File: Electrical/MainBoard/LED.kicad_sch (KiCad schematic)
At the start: 19 parts, among them U5 GSF7002DW, U6 GSF7002DW, U7 GSF7002DW, U8 GSF7002DW

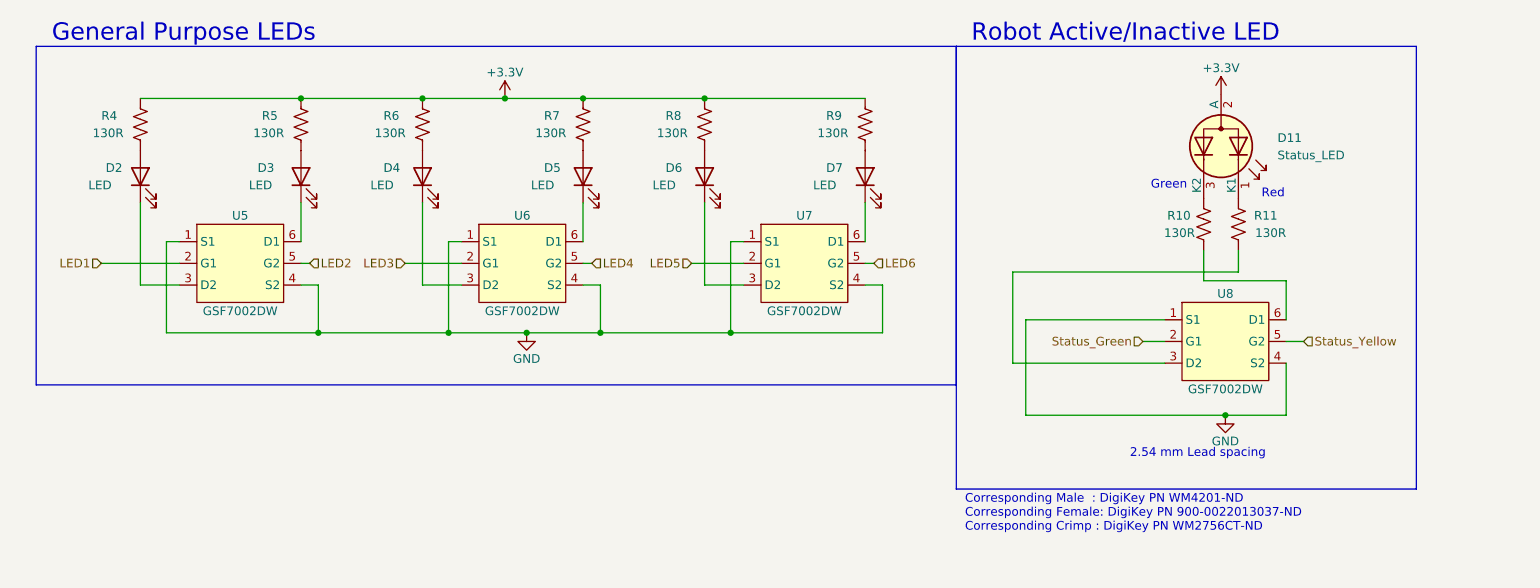
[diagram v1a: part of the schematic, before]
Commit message: Use more molex picoblades and make schematic prettier
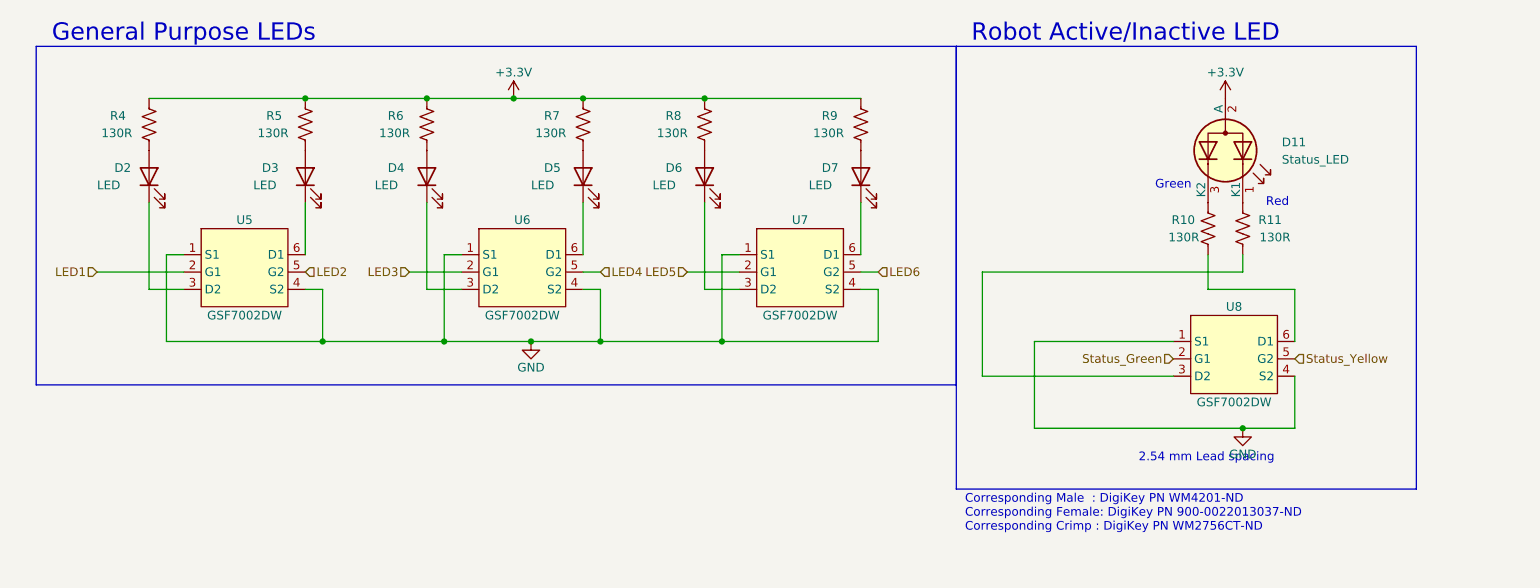
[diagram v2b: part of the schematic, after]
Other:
- moved on the sheet: D11, D2, D3, D4, D7, R10, R11, R4, R5, R6, R9, U5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
